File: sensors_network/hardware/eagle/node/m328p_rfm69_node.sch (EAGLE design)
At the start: 30 parts, among them IC2 L6920TSSOP8, U2 RFM69W, U3 ATMEGA328P, Y1 8MHz

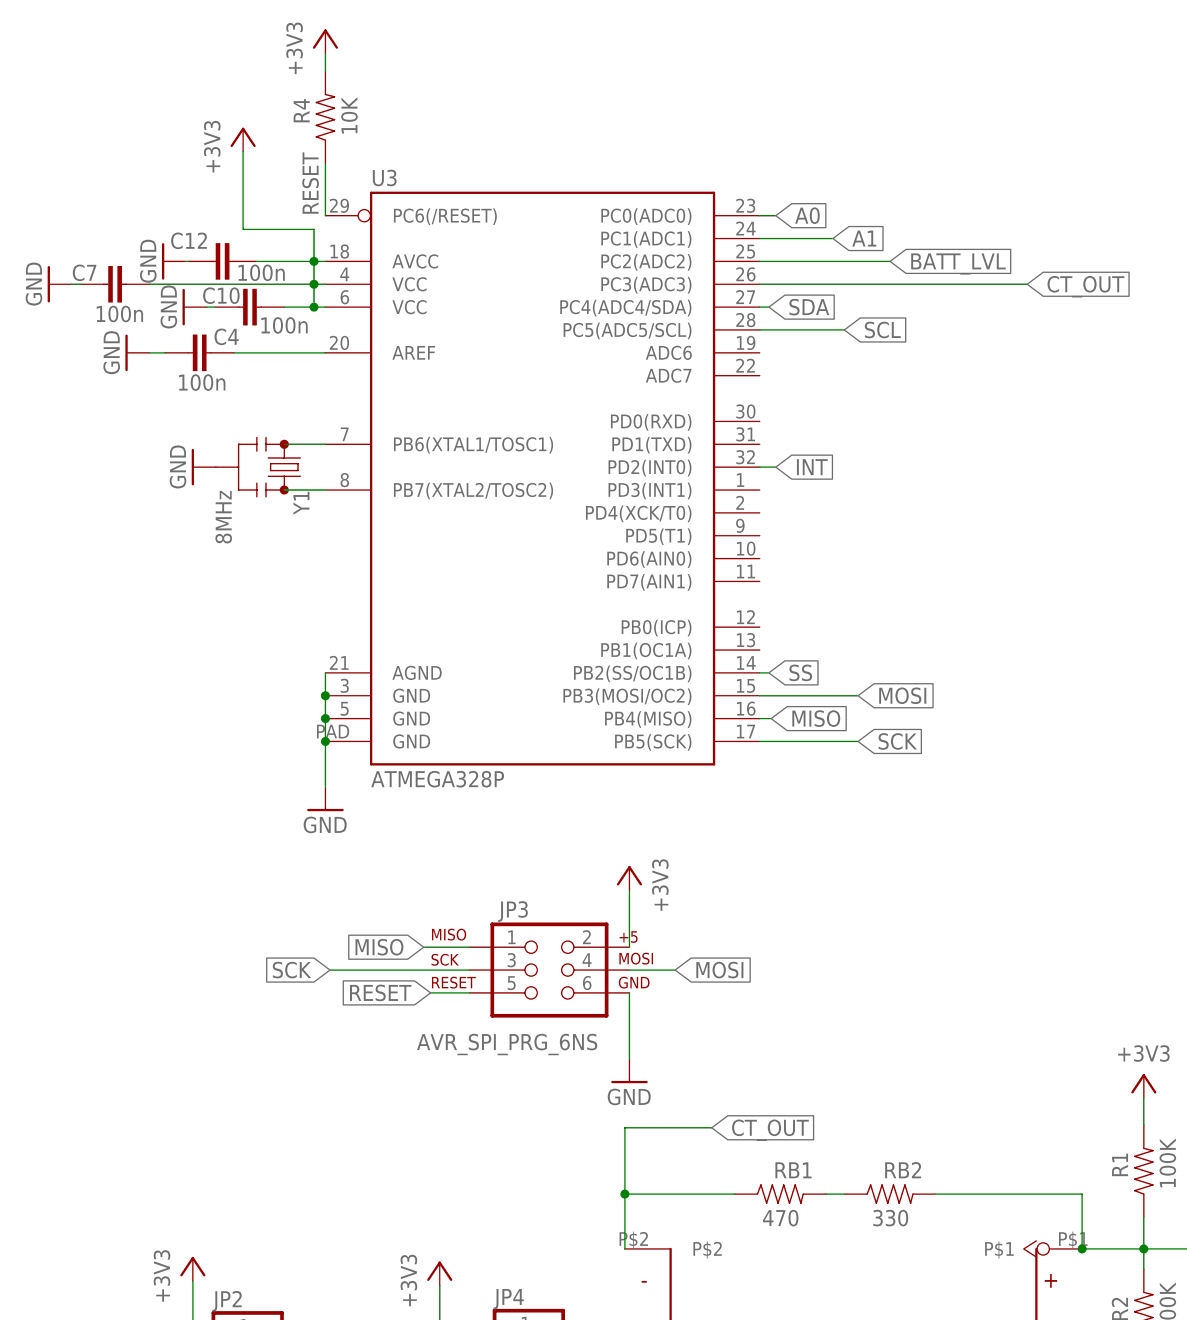
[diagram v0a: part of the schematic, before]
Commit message: [sensors network] Added sensor node eagle design - 2nd stage
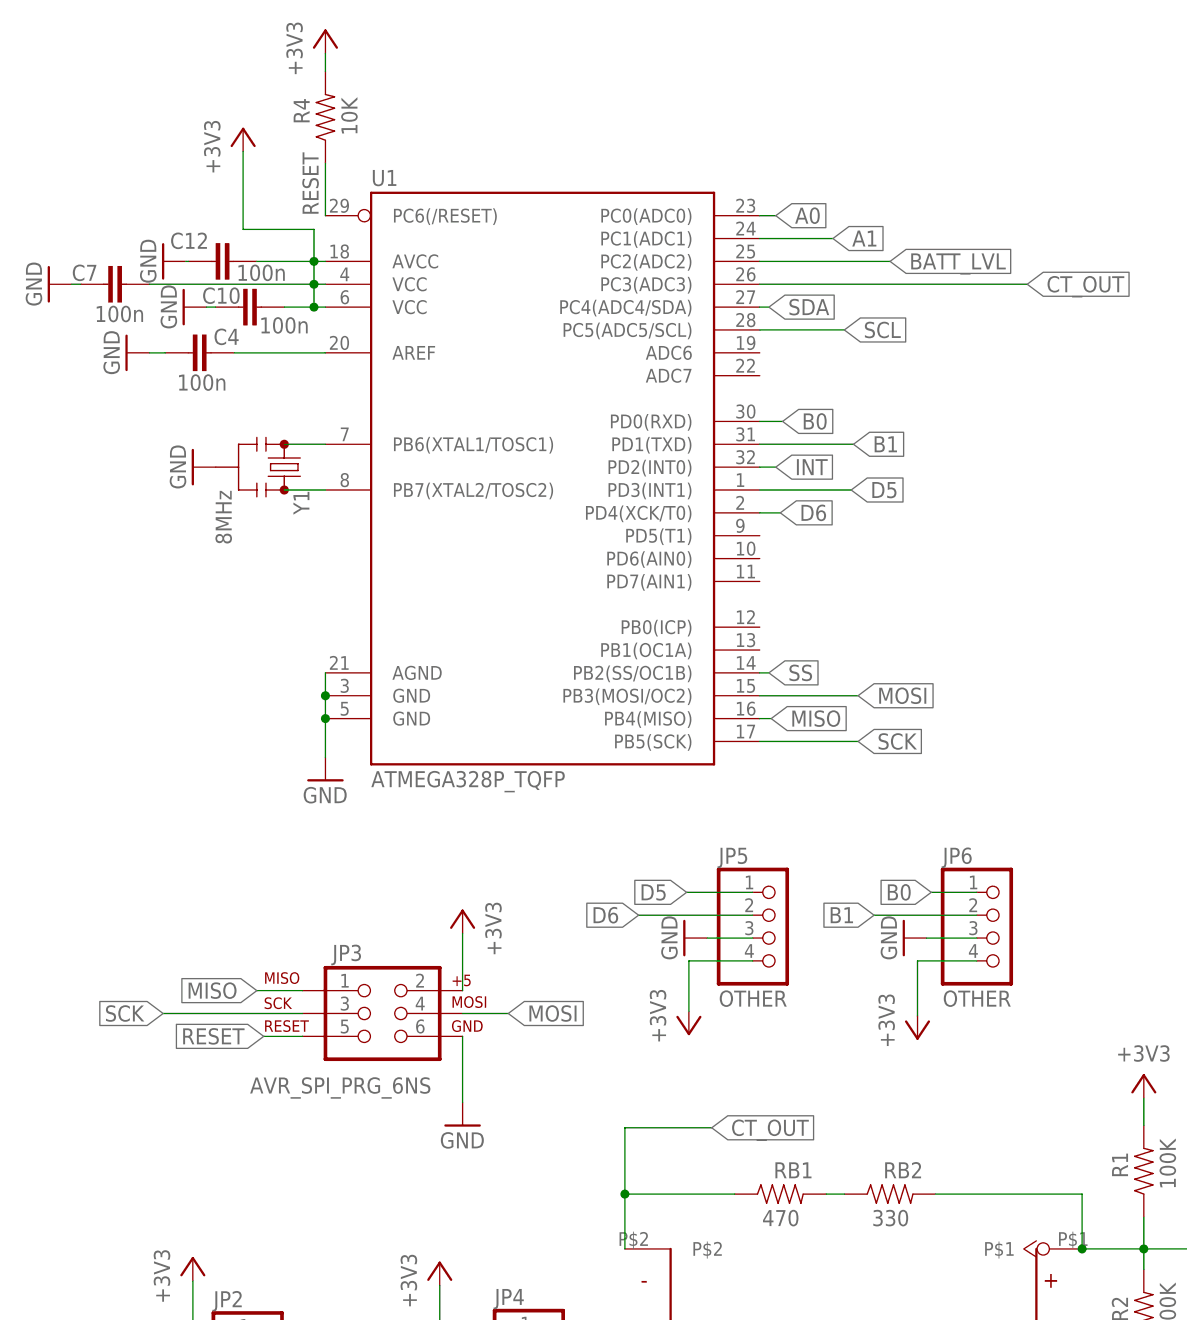
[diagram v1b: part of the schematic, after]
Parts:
- removed U3: ATMEGA328P, SparkFun-DigitalIC:ATMEGA328P_MLFMLF32
- added JP5, JP6: OTHER, pinhead:PINHD-1X4
- added U1: ATMEGA328P_TQFP, SparkFun-DigitalIC:ATMEGA328P_TQFP
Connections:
- new net B0: JP6.1, U1.PD0(RXD)
- new net B1: JP6.2, U1.PD1(TXD)
- new net D5: JP5.1, U1.PD3(INT1)
- new net D6: JP5.2, U1.PD4(XCK/T0)
- net +3V3: now also JP5.4, JP6.4, U1.AVCC, U1.VCC@4, U1.VCC@6; no longer U3.AVCC, U3.VCC@4, U3.VCC@6
- net A0: now also U1.PC0(ADC0); no longer U3.PC0(ADC0)
- net A1: now also U1.PC1(ADC1); no longer U3.PC1(ADC1)
- net BATT_LVL: now also U1.PC2(ADC2); no longer U3.PC2(ADC2)
- net CT_OUT: now also U1.PC3(ADC3); no longer U3.PC3(ADC3)
- net GND: now also JP5.3, JP6.3, U1.AGND, U1.GND@3, U1.GND@5; no longer U3.AGND, U3.GND@3, U3.GND@5, U3.GND@PAD
- net INT: now also U1.PD2(INT0); no longer U3.PD2(INT0)
- net MISO: now also U1.PB4(MISO); no longer U3.PB4(MISO)
- net MOSI: now also U1.PB3(MOSI/OC2); no longer U3.PB3(MOSI/OC2)
- net N$12: now also U1.AREF; no longer U3.AREF
- net N$6: now also U1.PB7(XTAL2/TOSC2); no longer U3.PB7(XTAL2/TOSC2)
- net N$9: now also U1.PB6(XTAL1/TOSC1); no longer U3.PB6(XTAL1/TOSC1)
- net RESET: now also U1.PC6(/RESET); no longer U3.PC6(/RESET)
- net SCK: now also U1.PB5(SCK); no longer U3.PB5(SCK)
- net SCL: now also U1.PC5(ADC5/SCL); no longer U3.PC5(ADC5/SCL)
- net SDA: now also U1.PC4(ADC4/SDA); no longer U3.PC4(ADC4/SDA)
- net SS: now also U1.PB2(SS/OC1B); no longer U3.PB2(SS/OC1B)
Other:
- moved on the sheet: JP3

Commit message: [sensors network] Worked sensor node eagle design - 3rd stage
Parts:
- JP1: device pinhead:PINHD-1X1 -> SparkFun-Connectors:M01SMD
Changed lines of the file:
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@@
 <part name="GND11" library="supply1" deviceset="GND" device=""/>
 <part name="+3V6" library="supply1" deviceset="+3V3" device=""/>
-<part name="JP1" library="pinhead" deviceset="PINHD-1X1" device="" value="ANT"/>
+<part name="JP1" library="SparkFun-Connectors" deviceset="M01" device="SMD" value="ANT"/>
 <part name="+3V7" library="supply1" deviceset="+3V3" device=""/>
 <part name="GND8" library="supply1" deviceset="GND" device=""/>
@@
 <instance part="GND11" gate="1" x="53.848" y="48.514"/>
 <instance part="+3V6" gate="G$1" x="53.848" y="72.39" rot="MR0"/>
-<instance part="JP1" gate="G$1" x="228.6" y="133.858"/>
+<instance part="JP1" gate="G$1" x="226.314" y="133.858" rot="R180"/>
 <instance part="+3V7" gate="G$1" x="23.876" y="33.782"/>
 <instance part="GND8" gate="1" x="22.86" y="22.606" rot="R270"/>
@@
 <pinref part="U2" gate="G$1" pin="ANT"/>
 <pinref part="JP1" gate="G$1" pin="1"/>
-<wire x1="226.06" y1="133.858" x2="208.28" y2="133.858" width="0.1524" layer="91"/>
-</segment>
-</net>
+<wire x1="218.694" y1="133.858" x2="208.28" y2="133.858" width="0.1524" layer="91"/>
+</segment>
+</net>

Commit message: [sensors network] Worked sensor node eagle design - 4th stage
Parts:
- IC2: value L6920TSSOP8 -> L6920
- JP3: value AVR_SPI_PRG_6NS -> ISP
- U1: value ATMEGA328P_TQFP -> M328P
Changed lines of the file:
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@@
 <part name="C9" library="SparkFun-Capacitors" deviceset="47UF-TANT" device="" value="47uF"/>
 <part name="L1" library="dlj-4018" deviceset="DLJ-4018" device="" value="10uH"/>
-<part name="IC2" library="l6920" deviceset="L6920" device="TSSOP8" value="L6920TSSOP8"/>
+<part name="IC2" library="l6920" deviceset="L6920" device="TSSOP8" value="L6920"/>
 <part name="GND2" library="supply1" deviceset="GND" device=""/>
 <part name="GND3" library="supply1" deviceset="GND" device=""/>
@@
 <part name="Y1" library="SparkFun-FreqCtrl" deviceset="RESONATOR" device="4MHZ" value="8MHz"/>
 <part name="GND10" library="supply1" deviceset="GND" device=""/>
-<part name="JP3" library="SparkFun-Connectors" deviceset="AVR_SPI_PRG_6" device="NS"/>
+<part name="JP3" library="SparkFun-Connectors" deviceset="AVR_SPI_PRG_6" device="NS" value="ISP"/>
 <part name="GND11" library="supply1" deviceset="GND" device=""/>
 <part name="+3V6" library="supply1" deviceset="+3V3" device=""/>
@@
 <part name="R1" library="SparkFun-Resistors" deviceset="RESISTOR" device="0805-RES" value="100K"/>
 <part name="R2" library="SparkFun-Resistors" deviceset="RESISTOR" device="0805-RES" value="100K"/>
-<part name="U1" library="SparkFun-DigitalIC" deviceset="ATMEGA328P_TQFP" device="" value="ATMEGA328P_TQFP"/>
+<part name="U1" library="SparkFun-DigitalIC" deviceset="ATMEGA328P_TQFP" device="" value="M328P"/>
 <part name="JP5" library="pinhead" deviceset="PINHD-1X4" device="" value="OTHER"/>
 <part name="JP6" library="pinhead" deviceset="PINHD-1X4" device="" value="OTHER"/>
@@
 </sheet>
 </sheets>
+<errors>
+</errors>
 </schematic>
 </drawing>

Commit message: [sensors network] Worked sensor node eagle design - 5th stage
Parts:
- JP1: value ANT -> ANTENNA
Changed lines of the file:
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@@
 <part name="GND11" library="supply1" deviceset="GND" device=""/>
 <part name="+3V6" library="supply1" deviceset="+3V3" device=""/>
-<part name="JP1" library="SparkFun-Connectors" deviceset="M01" device="SMD" value="ANT"/>
+<part name="JP1" library="SparkFun-Connectors" deviceset="M01" device="SMD" value="ANTENNA"/>
 <part name="+3V7" library="supply1" deviceset="+3V3" device=""/>
 <part name="GND8" library="supply1" deviceset="GND" device=""/>

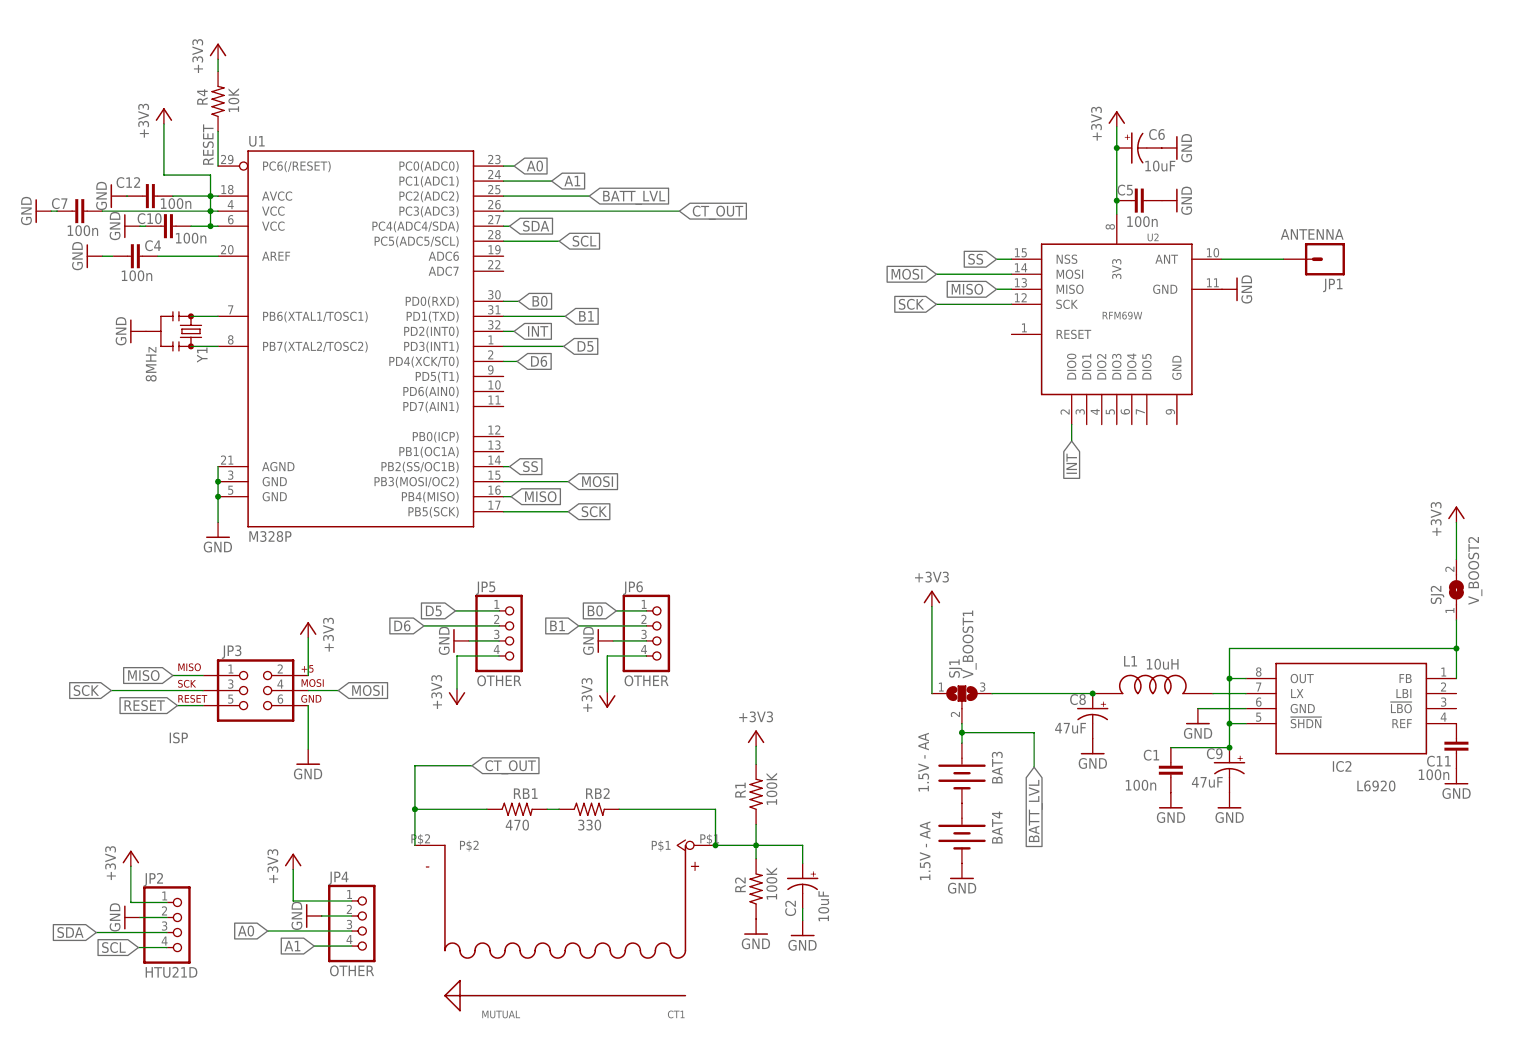
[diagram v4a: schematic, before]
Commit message: [sensors network] added sections to schematic
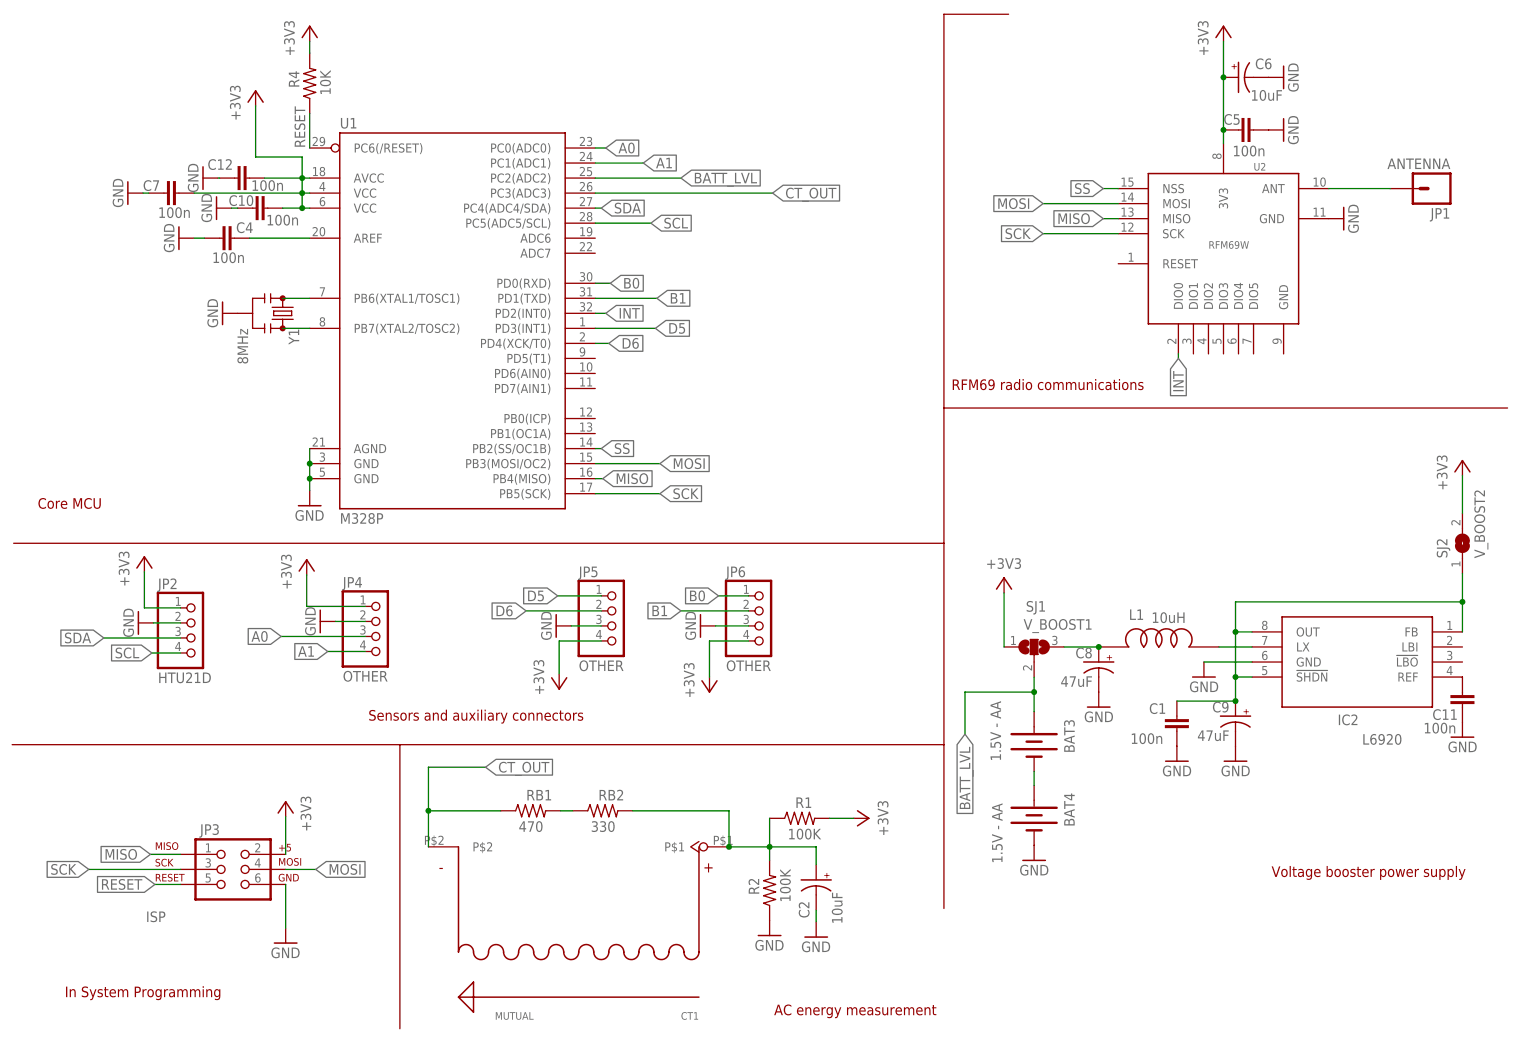
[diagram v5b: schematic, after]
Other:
- note added: "AC energy measurement"
- note added: "Core MCU"
- note added: "In System Programming"
- note added: "RFM69 radio communications"
- note added: "Sensors and auxiliary connectors"
- note added: "Voltage booster power supply"
- moved on the sheet: BAT3, BAT4, C1, C10, C11, C12, C2, C4, C5, C6, C7, C8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
